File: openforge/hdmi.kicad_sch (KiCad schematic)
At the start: 37 parts, among them P6 10118241-001RLF, U11 TDA19988BHN_C1_557

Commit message: added footprint associations
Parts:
- R146, R147, R148, R149, R158, R166: footprint (none) -> Resistor_SMD:R_0402_1005Metric
- RT1: footprint (none) -> footprints:FUS_RXEF010_TYCO_TYC
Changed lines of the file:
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@@
 			)
 		)
-		(property "Footprint" ""
+		(property "Footprint" "Resistor_SMD:R_0402_1005Metric"
 			(at 224.79 143.002 90)
 			(effects
@@
 			)
 		)
-		(property "Footprint" ""
+		(property "Footprint" "Resistor_SMD:R_0402_1005Metric"
 			(at 231.14 153.162 90)
 			(effects
@@
 			)
 		)
-		(property "Footprint" ""
+		(property "Footprint" "Resistor_SMD:R_0402_1005Metric"
 			(at 196.85 66.802 90)
 			(effects
@@
 			)
 		)
-		(property "Footprint" ""
+		(property "Footprint" "Resistor_SMD:R_0402_1005Metric"
 			(at 181.102 176.53 90)
 			(effects
@@
 			)
 		)
-		(property "Footprint" ""
+		(property "Footprint" "Resistor_SMD:R_0402_1005Metric"
 			(at 224.79 140.462 90)
 			(effects
@@
 			)
 		)
-		(property "Footprint" ""
+		(property "Footprint" "footprints:FUS_RXEF010_TYCO_TYC"
 			(at 372.11 44.45 0)
 			(effects
@@
 			)
 		)
-		(property "Footprint" ""
+		(property "Footprint" "Resistor_SMD:R_0402_1005Metric"
 			(at 224.79 145.542 90)
 			(effects

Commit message: Completed footprint association. Partially placed top side components on PCB
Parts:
- U11: footprint TDA19988BHN_C1_557:QFN50P900X900X100-65N -> footprints:QFN50P900X900X100-65N
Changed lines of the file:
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@@
 			)
 		)
-		(property "Footprint" "TDA19988BHN_C1_557:QFN50P900X900X100-65N"
+		(property "Footprint" "footprints:QFN50P900X900X100-65N"
 			(at 146.05 101.6 0)
 			(effects

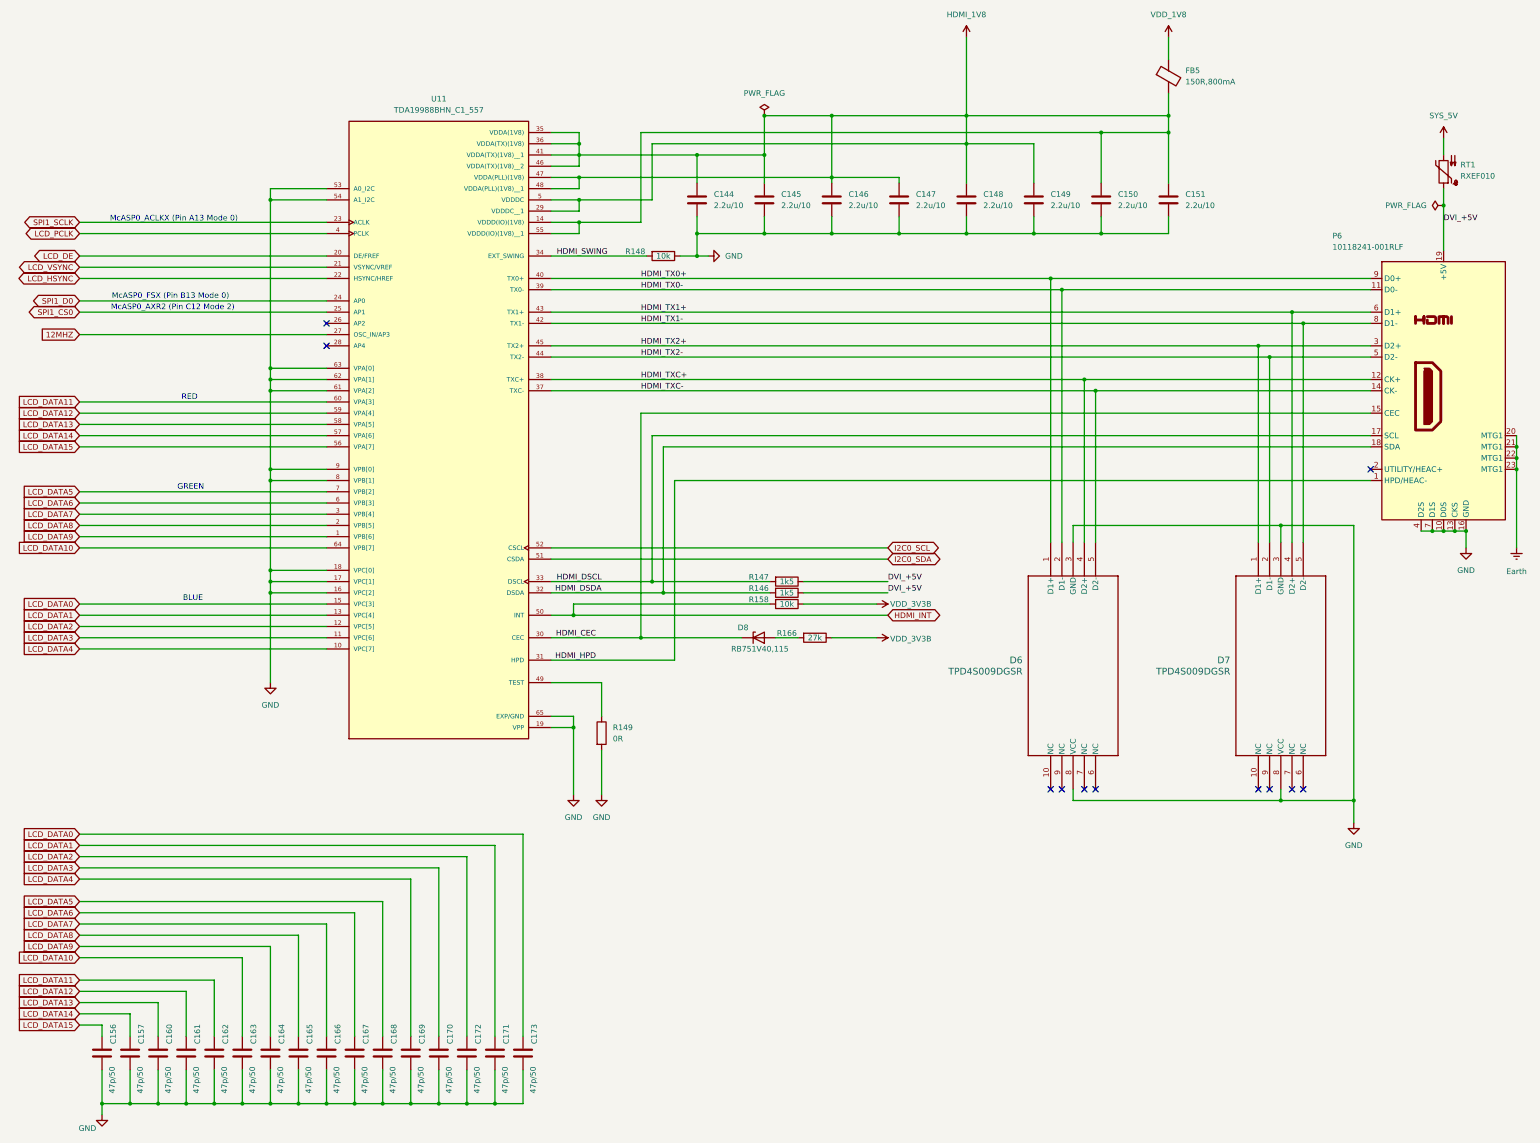
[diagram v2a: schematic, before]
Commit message: PCB all layers copied from beaglebone black
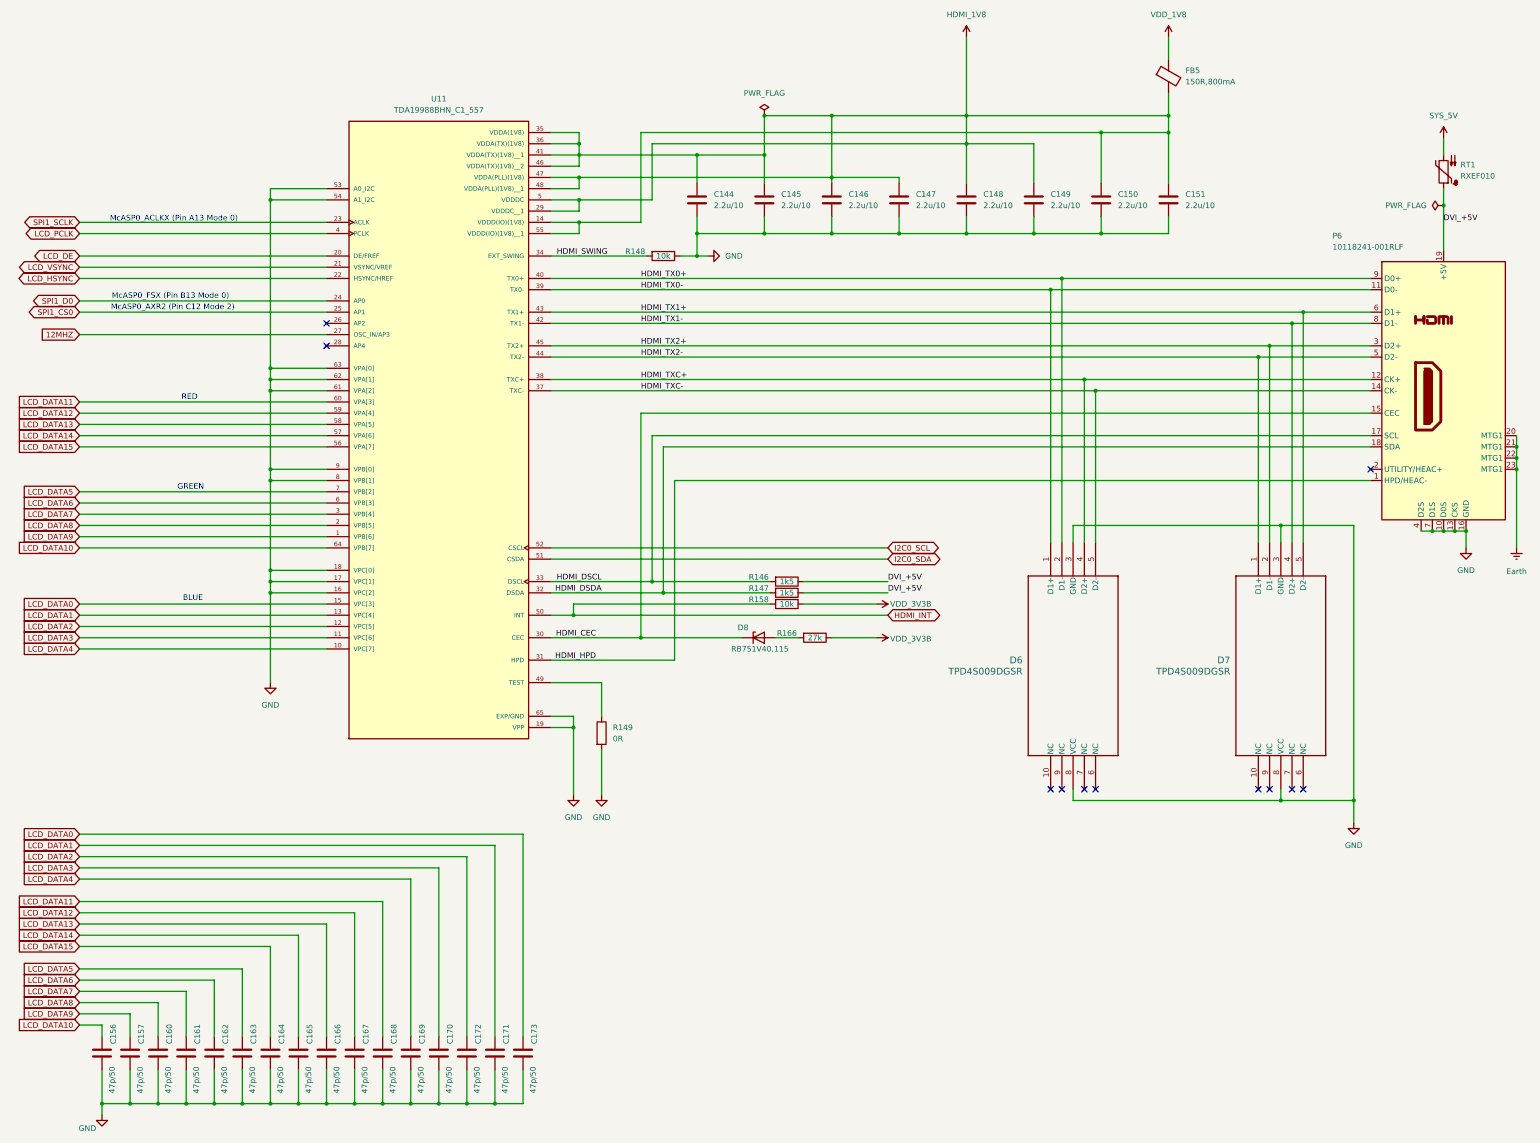
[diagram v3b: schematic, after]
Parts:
- RT1: footprint footprints:FUS_RXEF010_TYCO_TYC -> footprints:rxef010
- renumbered R147 to R146, R146 to R147
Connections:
- net HDMI_TX0+: now also D6.2 (D1-); no longer D6.1 (D1+)
- net HDMI_TX0-: now also D6.1 (D1+); no longer D6.2 (D1-)
- net HDMI_TX1+: now also D7.5 (D2-); no longer D7.4 (D2+)
- net HDMI_TX1-: now also D7.4 (D2+); no longer D7.5 (D2-)
- net HDMI_TX2+: now also D7.2 (D1-); no longer D7.1 (D1+)
- net HDMI_TX2-: now also D7.1 (D1+); no longer D7.2 (D1-)
- net LCD_DATA10: now also C156.1; no longer C163.1
- net LCD_DATA11: now also C168.1; no longer C162.1
- net LCD_DATA12: now also C167.1; no longer C161.1
- net LCD_DATA13: now also C166.1; no longer C160.1
- net LCD_DATA14: now also C165.1; no longer C157.1
- net LCD_DATA15: now also C164.1; no longer C156.1
- net LCD_DATA5: now also C163.1; no longer C168.1
- net LCD_DATA6: now also C162.1; no longer C167.1
- net LCD_DATA7: now also C161.1; no longer C166.1
- net LCD_DATA8: now also C160.1; no longer C165.1
- net LCD_DATA9: now also C157.1; no longer C164.1

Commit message: fixed all errors and major warnings
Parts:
- C144, C145, C146, C147, C148, C149, C150, C151, C156, C157, C160, C161, C162, C163, C164, C165, C166, C167, C168, C169, C170, C171, C172, C173: footprint Capacitor_SMD:C_0402_1005Metric -> footprints:C_0402_1005Metric
- R146, R147, R148, R149, R158, R166: footprint Resistor_SMD:R_0402_1005Metric -> footprints:R_0402_1005Metric
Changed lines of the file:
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@@
 			)
 		)
-		(property "Footprint" "Resistor_SMD:R_0402_1005Metric"
+		(property "Footprint" "footprints:R_0402_1005Metric"
 			(at 224.79 143.002 90)
 			(effects
@@
 			)
 		)
-		(property "Footprint" "Capacitor_SMD:C_0402_1005Metric"
+		(property "Footprint" "footprints:C_0402_1005Metric"
 			(at 205.4352 59.69 0)
 			(effects
@@
 			)
 		)
-		(property "Footprint" "Capacitor_SMD:C_0402_1005Metric"
+		(property "Footprint" "footprints:C_0402_1005Metric"
 			(at 140.6652 252.73 0)
 			(effects
@@
 			)
 		)
-		(property "Footprint" "Capacitor_SMD:C_0402_1005Metric"
+		(property "Footprint" "footprints:C_0402_1005Metric"
 			(at 108.9152 252.73 0)
 			(effects
@@
 			)
 		)
-		(property "Footprint" "Capacitor_SMD:C_0402_1005Metric"
+		(property "Footprint" "footprints:C_0402_1005Metric"
 			(at 89.8652 252.73 0)
 			(effects
@@
 			)
 		)
-		(property "Footprint" "Capacitor_SMD:C_0402_1005Metric"
+		(property "Footprint" "footprints:C_0402_1005Metric"
 			(at 166.0652 252.73 0)
 			(effects
@@
 			)
 		)
-		(property "Footprint" "Capacitor_SMD:C_0402_1005Metric"
+		(property "Footprint" "footprints:C_0402_1005Metric"
 			(at 153.3652 252.73 0)
 			(effects
@@
 			)
 		)
-		(property "Footprint" "Capacitor_SMD:C_0402_1005Metric"
+		(property "Footprint" "footprints:C_0402_1005Metric"
 			(at 251.1552 59.69 0)
 			(effects
@@
 			)
 		)
-		(property "Footprint" "Capacitor_SMD:C_0402_1005Metric"
+		(property "Footprint" "footprints:C_0402_1005Metric"
 			(at 70.8152 252.73 0)
 			(effects
@@
 			)
 		)
-		(property "Footprint" "Capacitor_SMD:C_0402_1005Metric"
+		(property "Footprint" "footprints:C_0402_1005Metric"
 			(at 77.1652 252.73 0)
 			(effects
@@
 			)
 		)
-		(property "Footprint" "Capacitor_SMD:C_0402_1005Metric"
+		(property "Footprint" "footprints:C_0402_1005Metric"
 			(at 134.3152 252.73 0)
 			(effects
@@
 			)
 		)
-		(property "Footprint" "Capacitor_SMD:C_0402_1005Metric"
+		(property "Footprint" "footprints:C_0402_1005Metric"
 			(at 266.3952 59.69 0)
 			(effects
@@
 			)
 		)
-		(property "Footprint" "Resistor_SMD:R_0402_1005Metric"
+		(property "Footprint" "footprints:R_0402_1005Metric"
 			(at 231.14 153.162 90)
 			(effects
@@
 			)
 		)
-		(property "Footprint" "Capacitor_SMD:C_0402_1005Metric"
+		(property "Footprint" "footprints:C_0402_1005Metric"
 			(at 147.0152 252.73 0)
 			(effects
@@
 			)
 		)
-		(property "Footprint" "Capacitor_SMD:C_0402_1005Metric"
+		(property "Footprint" "footprints:C_0402_1005Metric"
 			(at 220.6752 59.69 0)
 			(effects
@@
 			)
 		)
-		(property "Footprint" "Resistor_SMD:R_0402_1005Metric"
+		(property "Footprint" "footprints:R_0402_1005Metric"
 			(at 196.85 66.802 90)
 			(effects
@@
 			)
 		)
-		(property "Footprint" "Capacitor_SMD:C_0402_1005Metric"
+		(property "Footprint" "footprints:C_0402_1005Metric"
 			(at 83.5152 252.73 0)
 			(effects
@@
 			)
 		)
-		(property "Footprint" "Capacitor_SMD:C_0402_1005Metric"
+		(property "Footprint" "footprints:C_0402_1005Metric"
 			(at 159.7152 252.73 0)
 			(effects
@@
 			)
 		)
-		(property "Footprint" "Capacitor_SMD:C_0402_1005Metric"
+		(property "Footprint" "footprints:C_0402_1005Metric"
 			(at 127.9652 252.73 0)
 			(effects
@@
 			)
 		)
-		(property "Footprint" "Capacitor_SMD:C_0402_1005Metric"
+		(property "Footprint" "footprints:C_0402_1005Metric"
 			(at 121.6152 252.73 0)
 			(effects
@@
 			)
 		)
-		(property "Footprint" "Resistor_SMD:R_0402_1005Metric"
+		(property "Footprint" "footprints:R_0402_1005Metric"
 			(at 181.102 176.53 90)
 			(effects
@@
 			)
 		)
-		(property "Footprint" "Capacitor_SMD:C_0402_1005Metric"
+		(property "Footprint" "footprints:C_0402_1005Metric"
 			(at 96.2152 252.73 0)
 			(effects
@@
 			)
 		)
-		(property "Footprint" "Capacitor_SMD:C_0402_1005Metric"
+		(property "Footprint" "footprints:C_0402_1005Metric"
 			(at 281.6352 59.69 0)
 			(effects
@@
 			)
 		)
-		(property "Footprint" "Resistor_SMD:R_0402_1005Metric"
+		(property "Footprint" "footprints:R_0402_1005Metric"
 			(at 224.79 140.462 90)
 			(effects
@@
 			)
 		)
-		(property "Footprint" "Capacitor_SMD:C_0402_1005Metric"
+		(property "Footprint" "footprints:C_0402_1005Metric"
 			(at 312.1152 59.69 0)
 			(effects
@@
 			)
 		)
-		(property "Footprint" "Capacitor_SMD:C_0402_1005Metric"
+		(property "Footprint" "footprints:C_0402_1005Metric"
 			(at 102.5652 252.73 0)
 			(effects
@@
 			)
 		)
-		(property "Footprint" "Capacitor_SMD:C_0402_1005Metric"
+		(property "Footprint" "footprints:C_0402_1005Metric"
 			(at 296.8752 59.69 0)
 			(effects
@@
 			)
 		)
-		(property "Footprint" "Capacitor_SMD:C_0402_1005Metric"
+		(property "Footprint" "footprints:C_0402_1005Metric"
 			(at 115.2652 252.73 0)
 			(effects
@@
 			)
 		)
-		(property "Footprint" "Resistor_SMD:R_0402_1005Metric"
+		(property "Footprint" "footprints:R_0402_1005Metric"
 			(at 224.79 145.542 90)
 			(effects
@@
 			)
 		)
-		(property "Footprint" "Capacitor_SMD:C_0402_1005Metric"
+		(property "Footprint" "footprints:C_0402_1005Metric"
 			(at 235.9152 59.69 0)
 			(effects
